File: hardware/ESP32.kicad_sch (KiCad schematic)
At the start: 17 parts, among them J1 USB_C_Receptacle_USB2.0_16P, SW1 SW_Omron_B3FS, SW2 SW_Omron_B3FS, U2 ESP32-C3-WROOM-02, U8 USBLC6-2SC6

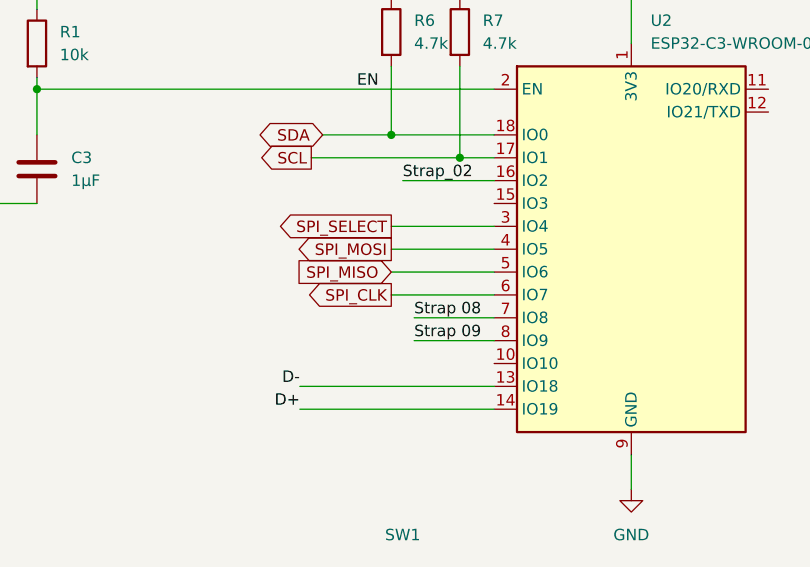
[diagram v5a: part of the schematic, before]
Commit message: Add BQ25798 debug pins to ESP and placed TP & headers
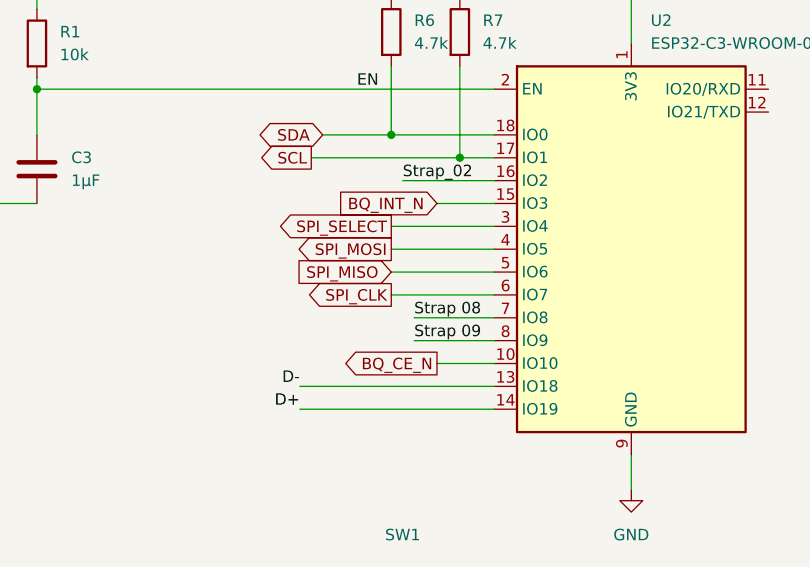
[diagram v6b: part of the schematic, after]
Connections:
- net BQ_CE_N: now reaches U2.10 (IO10)
- net BQ_INT_N: now reaches U2.15 (IO3)
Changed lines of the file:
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@@
+	(wire
+		(pts
+			(xy 191.77 58.42) (xy 198.12 58.42)
+		)
+		(stroke
+			(width 0)
+			(type default)
+		)
+	)
 	(wire
 		(pts
@@
 		(pts
 			(xy 134.62 36.83) (xy 134.62 31.75)
+		)
+		(stroke
+			(width 0)
+			(type default)
+		)
+	)
+	(wire
+		(pts
+			(xy 191.77 76.2) (xy 198.12 76.2)
 		)
 		(stroke
@@
 		)
 	)
+	(global_label "BQ_CE_N"
+		(shape output)
+		(at 191.77 76.2 180)
+		(fields_autoplaced yes)
+		(effects
+			(font
+				(size 1.27 1.27)
+			)
+			(justify right)
+		)
+		(property "Intersheetrefs" "${INTERSHEET_REFS}"
+			(at 180.4996 76.2 0)
+			(effects
+				(font
+					(size 1.27 1.27)
+				)
+				(justify right)
+				(hide yes)
+			)
+		)
+	)
 	(global_label "SPI_MISO"
 		(shape input)
@@
 				(hide yes)
 			)
+		)
+	)
+	(global_label "BQ_INT_N"
+		(shape input)
+		(at 191.77 58.42 180)
+		(fields_autoplaced yes)
+		(effects
+			(font
+				(size 1.27 1.27)
+			)
+			(justify right)
+		)
+		(property "Intersheetrefs" "${INTERSHEET_REFS}"
+			(at 180.0157 58.42 0)
+			(effects
+				(font
+					(size 1.27 1.27)
+				)
+				(justify right)
+				(hide yes)
+			)
